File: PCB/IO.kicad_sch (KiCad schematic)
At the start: 34 parts, among them J501 Conn_02x03_Counter_Clockwise, J502 USB_C_Receptacle_USB2.0_16P, J503 Screw_Terminal_01x06, J504 Screw_Terminal_01x04, J505 Conn_01x04, J506 Conn_02x03_Counter_Clockwise, J507 Conn_01x06, Q1 SL2302S

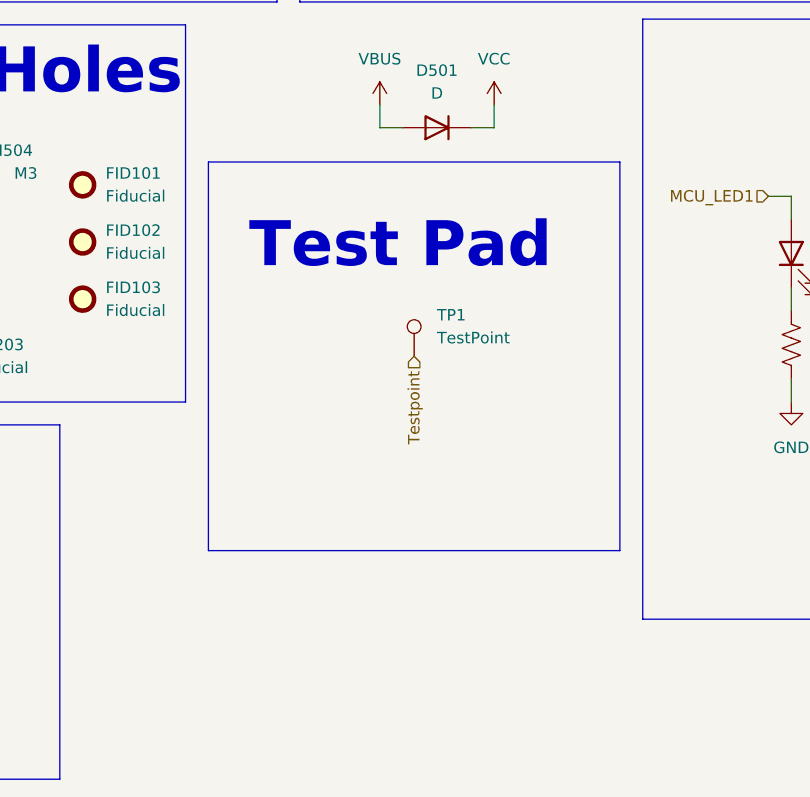
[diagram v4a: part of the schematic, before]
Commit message: Added DFU button and VCC pad by programming header
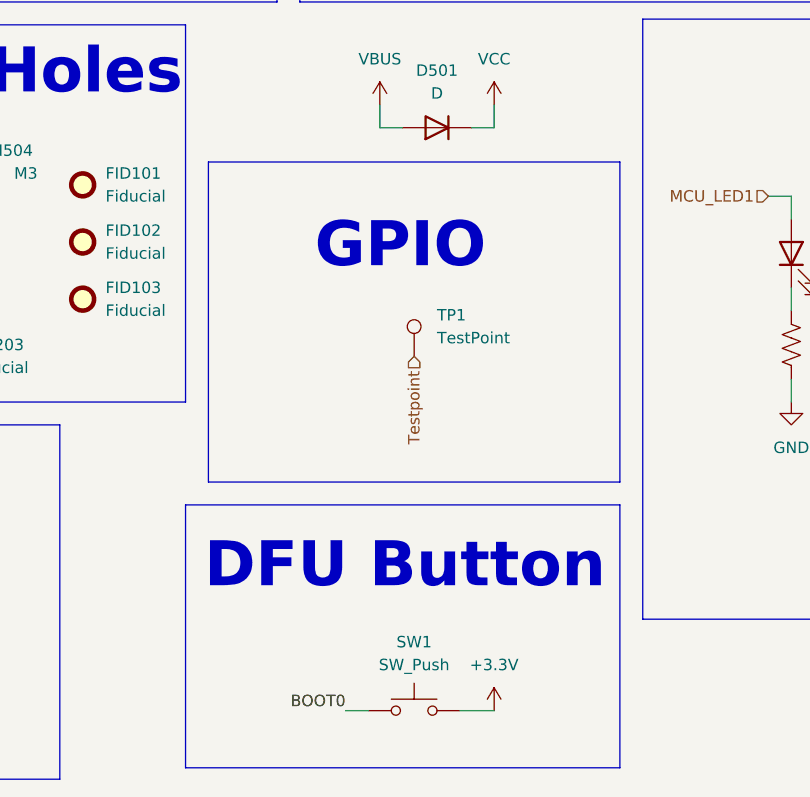
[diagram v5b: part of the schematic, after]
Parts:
- added SW1: SW_Push, imported:SW_1TS026A, symbol Switch:SW_Push
- TP1: footprint (none) -> TestPoint:TestPoint_Pad_D1.5mm
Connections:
- net +3.3V: now also SW1.2
- net BOOT0: now also SW1.1
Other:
- note added: "DFU Button"
- note added: "GPIO"
- note removed: "Test Pad"
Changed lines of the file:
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@@
 	(rectangle
 		(start 78.74 101.6)
-		(end 124.46 144.78)
+		(end 124.46 137.16)
 		(stroke
 			(width 0)
@@
 		)
 	)
+	(rectangle
+		(start 76.2 139.7)
+		(end 124.46 168.91)
+		(stroke
+			(width 0)
+			(type default)
+		)
+		(fill
+			(type none)
+		)
+	)
 	(text "Header"
 		(exclude_from_sim no)
@@
 		)
 	)
-	(text "Test Pad"
+	(text "GPIO"
 		(exclude_from_sim no)
 		(at 100.076 110.998 0)
@@
 		)
 	)
+	(text "DFU Button"
+		(exclude_from_sim no)
+		(at 100.584 146.558 0)
+		(effects
+			(font
+				(size 5 5)
+				(thickness 1)
+				(bold yes)
+			)
+		)
+	)
 	(text "Pyro Channels"
 		(exclude_from_sim no)
@@
 	(wire
 		(pts
+			(xy 106.68 162.56) (xy 110.49 162.56)
+		)
+		(stroke
+			(width 0)
+			(type default)
+		)
+	)
+	(wire
+		(pts
 			(xy 165.1 34.29) (xy 167.64 34.29)
 		)
@@
 	(wire
 		(pts
+			(xy 93.98 162.56) (xy 96.52 162.56)
+		)
+		(stroke
+			(width 0)
+			(type default)
+		)
+	)
+	(wire
+		(pts
 			(xy 74.93 53.34) (xy 72.39 53.34)
 		)
@@
 		)
 	)
+	(label "BOOT0"
+		(at 93.98 162.56 180)
+		(effects
+			(font
+				(size 1.27 1.27)
+			)
+			(justify right bottom)
+		)
+	)
 	(hierarchical_label "SWO"
 		(shape input)
@@
 	)
 	(symbol
+		(lib_id "power:+3.3V")
+		(at 110.49 162.56 0)
+		(unit 1)
+		(exclude_from_sim no)
+		(in_bom yes)
+		(on_board yes)
+		(dnp no)
+		(fields_autoplaced yes)
+		(property "Reference" "#PWR07"
+			(at 110.49 166.37 0)
+			(effects
+				(font
+					(size 1.27 1.27)
+				)
+				(hide yes)
+			)
+		)
+		(property "Value" "+3.3V"
+			(at 110.49 157.48 0)
+			(effects
+				(font
+					(size 1.27 1.27)
+				)
+			)
+		)
+		(property "Footprint" ""
+			(at 110.49 162.56 0)
+			(effects
+				(font
+					(size 1.27 1.27)
+				)
+				(hide yes)
+			)
+		)
+		(property "Datasheet" ""
+			(at 110.49 162.56 0)
+			(effects
+				(font
+					(size 1.27 1.27)
+				)
+				(hide yes)
+			)
+		)
+		(property "Description" "Power symbol creates a global label with name \"+3.3V\""
+			(at 110.49 162.56 0)
+			(effects
+				(font
+					(size 1.27 1.27)
+				)
+				(hide yes)
+			)
+		)
+		(pin "1"
+		)
+		(instances
+			(project "Flight Computer"
+				(path "/4254ccd1-49f4-4fe6-9bf7-ccb200d73af4/0a0b3d01-7422-42e0-b725-ff9e85b891ec"
+					(reference "#PWR07")
+					(unit 1)
+				)
+			)
+		)
+	)
+	(symbol
 		(lib_id "power:GND")
 		(at 36.83 110.49 0)
@@
 	)
 	(symbol
+		(lib_id "Switch:SW_Push")
+		(at 101.6 162.56 0)
+		(unit 1)
+		(exclude_from_sim no)
+		(in_bom yes)
+		(on_board yes)
+		(dnp no)
+		(fields_autoplaced yes)
+		(property "Reference" "SW1"
+			(at 101.6 154.94 0)
+			(effects
+				(font
+					(size 1.27 1.27)
+				)
+			)
+		)
+		(property "Value" "SW_Push"
+			(at 101.6 157.48 0)
+			(effects
+				(font
+					(size 1.27 1.27)
+				)
+			)
+		)
+		(property "Footprint" "imported:SW_1TS026A"
+			(at 101.6 157.48 0)
+			(effects
+				(font
+					(size 1.27 1.27)
+				)
+				(hide yes)
+			)
+		)
+		(property "Datasheet" "~"
+			(at 101.6 157.48 0)
+			(effects
+				(font
+					(size 1.27 1.27)
+				)
+				(hide yes)
+			)
+		)
+		(property "Description" "Push button switch, generic, two pins"
+			(at 101.6 162.56 0)
+			(effects
+				(font
+					(size 1.27 1.27)
+				)
+				(hide yes)
+			)
+		)
+		(pin "2"
+		)
+		(pin "1"
+		)
+		(instances
+			(project "Flight Computer"
+				(path "/4254ccd1-49f4-4fe6-9bf7-ccb200d73af4/0a0b3d01-7422-42e0-b725-ff9e85b891ec"
+					(reference "SW1")
+					(unit 1)
+				)
+			)
+		)
+	)
+	(symbol
 		(lib_id "Connector_Generic:Conn_01x06")
 		(at 27.94 154.94 0)
@@
 			)
 		)
-		(property "Footprint" ""
+		(property "Footprint" "TestPoint:TestPoint_Pad_D1.5mm"
 			(at 106.68 123.19 0)
 			(effects

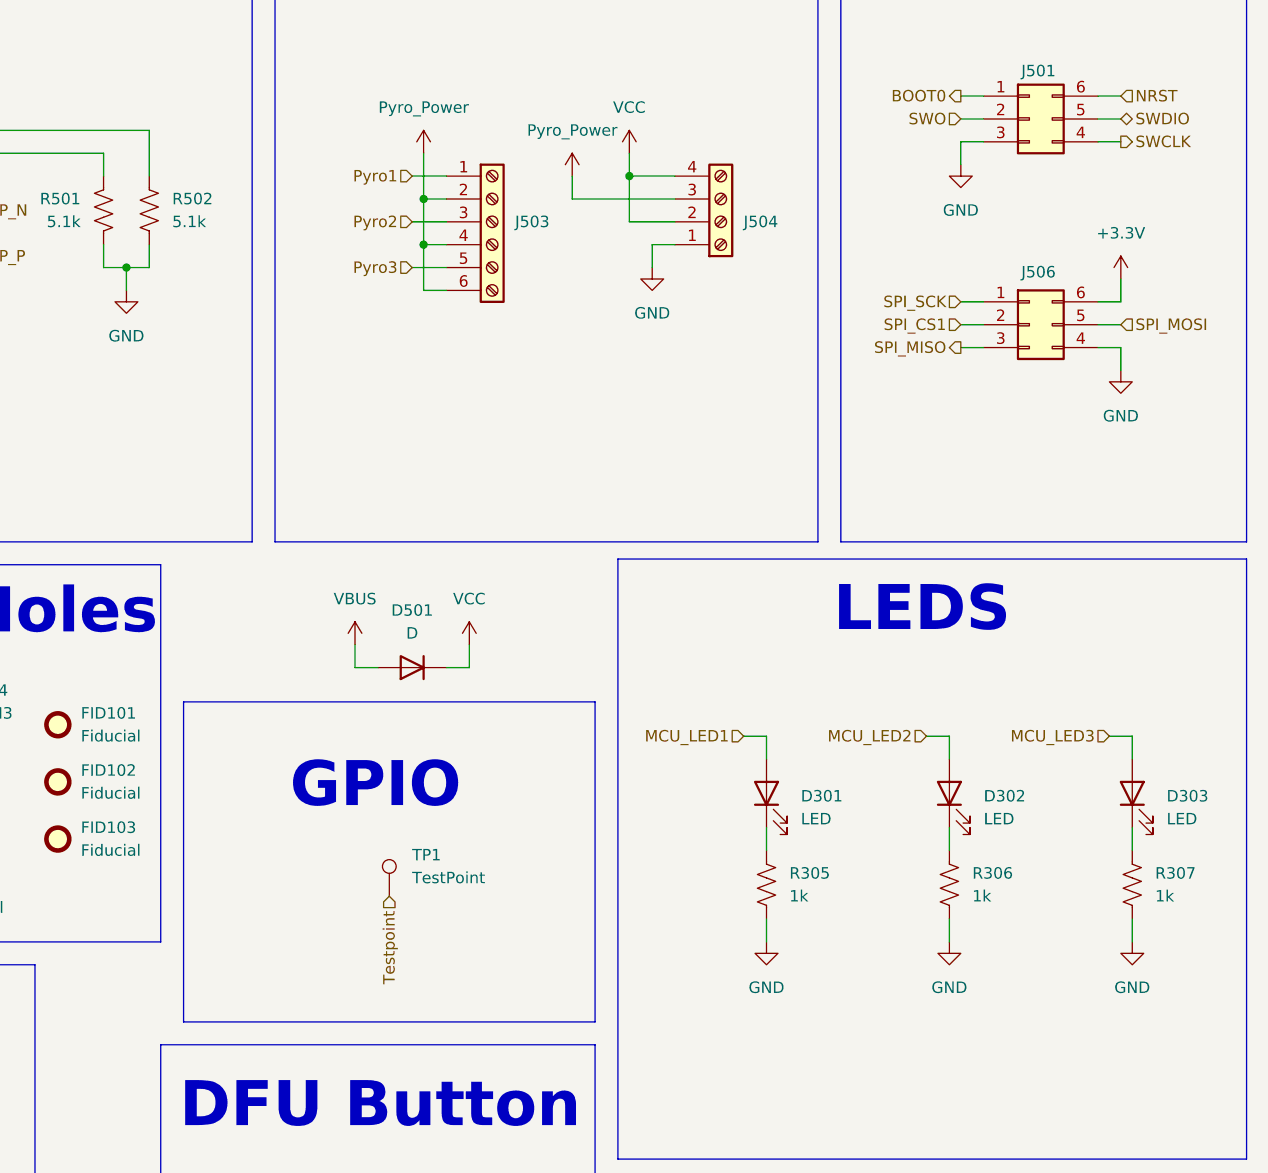
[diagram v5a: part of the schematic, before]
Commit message: Added two more GPIO test pads
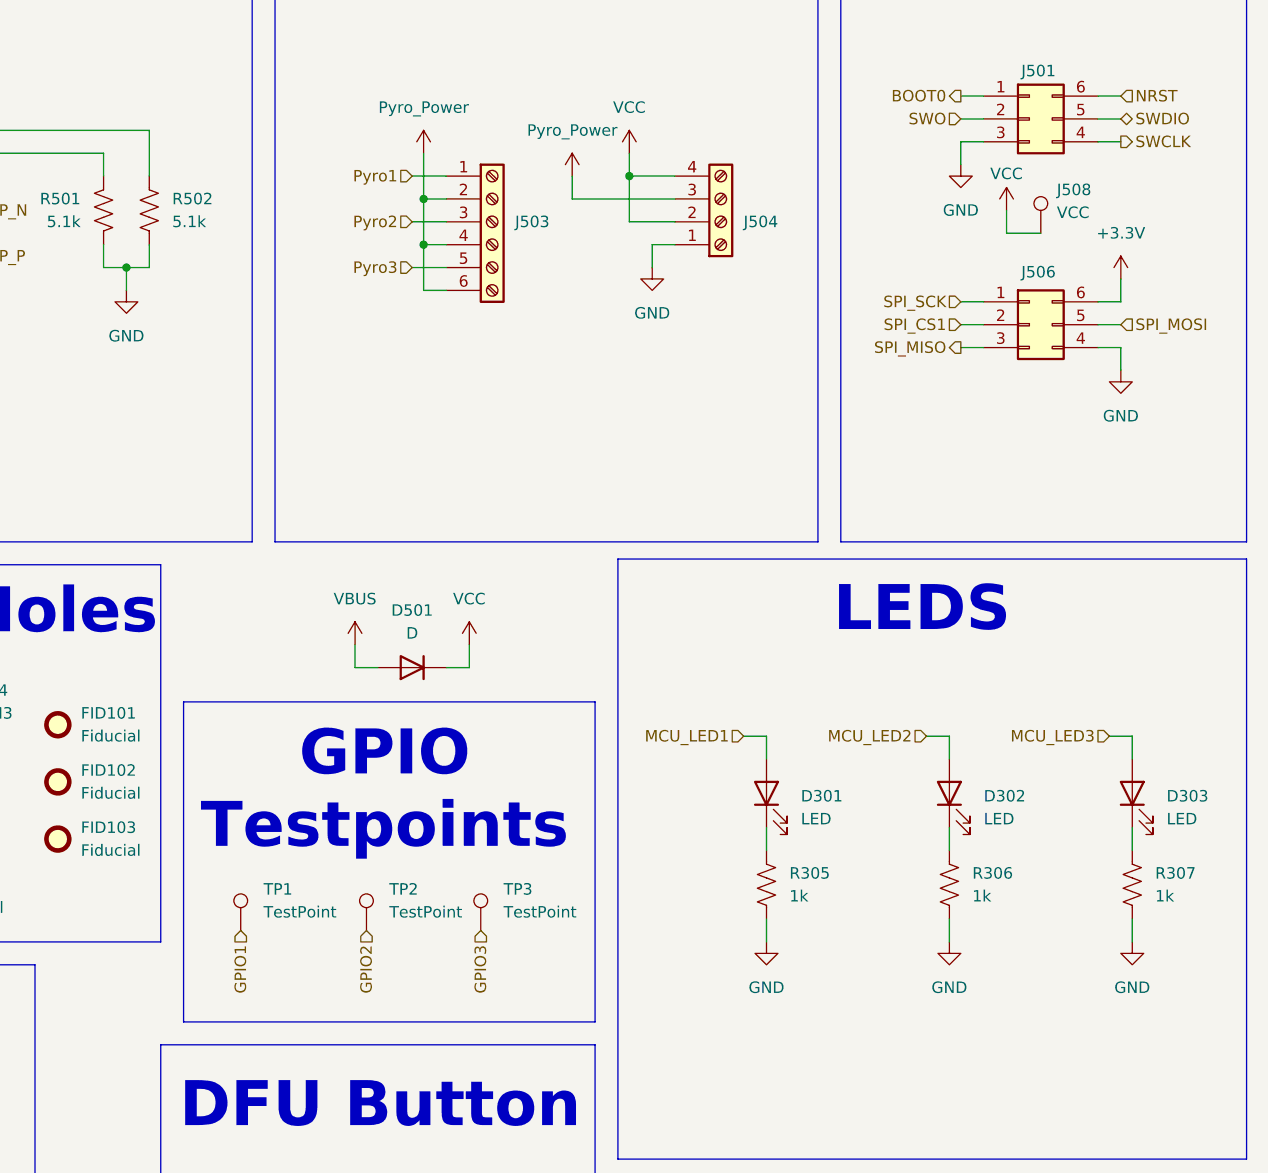
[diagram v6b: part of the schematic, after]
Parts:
- added J508: VCC, TestPoint:TestPoint_Pad_1.0x1.0mm, symbol Connector:TestPoint
- added TP2, TP3: TestPoint, TestPoint:TestPoint_Pad_D1.5mm, symbol Connector:TestPoint
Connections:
- net VCC: now also J508.1
- net Testpoint renamed GPIO1
- new net GPIO2: TP2.1
- new net GPIO3: TP3.1
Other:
- note added: "GPIO Testpoints"
- note removed: "GPIO"
- moved on the sheet: TP1

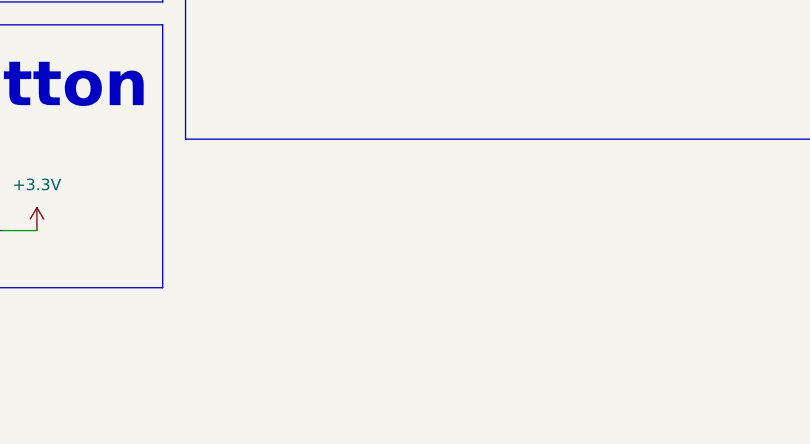
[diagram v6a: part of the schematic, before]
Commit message: Added Reset Button
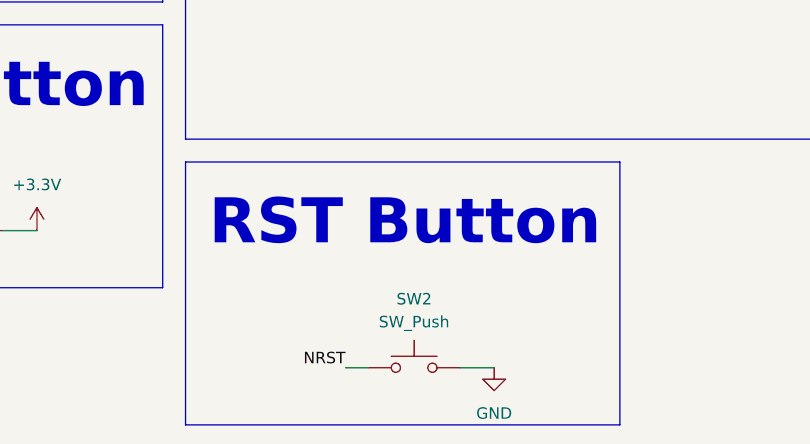
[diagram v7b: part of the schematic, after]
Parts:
- added SW2: SW_Push, imported:SW_1TS026A, symbol Switch:SW_Push
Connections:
- net GND: now also SW2.2
- net NRST: now also SW2.1
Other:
- note added: "RST Button"
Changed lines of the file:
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@@
 	)
 	(rectangle
+		(start 127 154.94)
+		(end 175.26 184.15)
+		(stroke
+			(width 0)
+			(type default)
+		)
+		(fill
+			(type none)
+		)
+	)
+	(rectangle
 		(start 151.765 14.605)
 		(end 196.85 83.82)
@@
 		)
 	)
+	(text "RST Button"
+		(exclude_from_sim no)
+		(at 151.384 161.798 0)
+		(effects
+			(font
+				(size 5 5)
+				(thickness 1)
+				(bold yes)
+			)
+		)
+	)
 	(text "Buzzer"
 		(exclude_from_sim no)
@@
 	(wire
 		(pts
+			(xy 157.48 177.8) (xy 161.29 177.8)
+		)
+		(stroke
+			(width 0)
+			(type default)
+		)
+	)
+	(wire
+		(pts
 			(xy 182.88 54.61) (xy 182.88 57.15)
 		)
@@
 	(wire
 		(pts
+			(xy 144.78 177.8) (xy 147.32 177.8)
+		)
+		(stroke
+			(width 0)
+			(type default)
+		)
+	)
+	(wire
+		(pts
 			(xy 220.98 48.26) (xy 223.52 48.26)
 		)
@@
 		)
 	)
+	(label "NRST"
+		(at 144.78 177.8 180)
+		(effects
+			(font
+				(size 1.27 1.27)
+			)
+			(justify right bottom)
+		)
+	)
 	(label "BOOT0"
 		(at 93.98 162.56 180)
@@
 		)
 		(instances
-			(project ""
+			(project "Flight Computer"
 				(path "/4254ccd1-49f4-4fe6-9bf7-ccb200d73af4/0a0b3d01-7422-42e0-b725-ff9e85b891ec"
 					(reference "J501")
@@
 		)
 		(instances
-			(project ""
+			(project "Flight Computer"
 				(path "/4254ccd1-49f4-4fe6-9bf7-ccb200d73af4/0a0b3d01-7422-42e0-b725-ff9e85b891ec"
 					(reference "BZ501")
@@
 		)
 		(instances
-			(project ""
+			(project "Flight Computer"
 				(path "/4254ccd1-49f4-4fe6-9bf7-ccb200d73af4/0a0b3d01-7422-42e0-b725-ff9e85b891ec"
 					(reference "#PWR0501")
@@
 		)
 		(instances
-			(project ""
+			(project "Flight Computer"
 				(path "/4254ccd1-49f4-4fe6-9bf7-ccb200d73af4/0a0b3d01-7422-42e0-b725-ff9e85b891ec"
 					(reference "G501")
@@
 		)
 		(instances
-			(project ""
+			(project "Flight Computer"
 				(path "/4254ccd1-49f4-4fe6-9bf7-ccb200d73af4/0a0b3d01-7422-42e0-b725-ff9e85b891ec"
 					(reference "J502")
@@
 		)
 		(instances
-			(project ""
+			(project "Flight Computer"
 				(path "/4254ccd1-49f4-4fe6-9bf7-ccb200d73af4/0a0b3d01-7422-42e0-b725-ff9e85b891ec"
 					(reference "J503")
@@
 		)
 		(instances
-			(project ""
+			(project "Flight Computer"
 				(path "/4254ccd1-49f4-4fe6-9bf7-ccb200d73af4/0a0b3d01-7422-42e0-b725-ff9e85b891ec"
 					(reference "R503")
@@
 		)
 		(instances
-			(project ""
+			(project "Flight Computer"
 				(path "/4254ccd1-49f4-4fe6-9bf7-ccb200d73af4/0a0b3d01-7422-42e0-b725-ff9e85b891ec"
 					(reference "#PWR0508")
@@
 	)
 	(symbol
+		(lib_id "Switch:SW_Push")
+		(at 152.4 177.8 0)
+		(unit 1)
+		(exclude_from_sim no)
+		(in_bom yes)
+		(on_board yes)
+		(dnp no)
+		(fields_autoplaced yes)
+		(property "Reference" "SW2"
+			(at 152.4 170.18 0)
+			(effects
+				(font
+					(size 1.27 1.27)
+				)
+			)
+		)
+		(property "Value" "SW_Push"
+			(at 152.4 172.72 0)
+			(effects
+				(font
+					(size 1.27 1.27)
+				)
+			)
+		)
+		(property "Footprint" "imported:SW_1TS026A"
+			(at 152.4 172.72 0)
+			(effects
+				(font
+					(size 1.27 1.27)
+				)
+				(hide yes)
+			)
+		)
+		(property "Datasheet" "~"
+			(at 152.4 172.72 0)
+			(effects
+				(font
+					(size 1.27 1.27)
+				)
+				(hide yes)
+			)
+		)
+		(property "Description" "Push button switch, generic, two pins"
+			(at 152.4 177.8 0)
+			(effects
+				(font
+					(size 1.27 1.27)
+				)
+				(hide yes)
+			)
+		)
+		(pin "2"
+		)
+		(pin "1"
+		)
+		(instances
+			(project "Flight Computer"
+				(path "/4254ccd1-49f4-4fe6-9bf7-ccb200d73af4/0a0b3d01-7422-42e0-b725-ff9e85b891ec"
+					(reference "SW2")
+					(unit 1)
+				)
+			)
+		)
+	)
+	(symbol
 		(lib_id "Connector:TestPoint")
 		(at 85.09 127 0)
@@
 		)
 		(instances
-			(project ""
+			(project "Flight Computer"
 				(path "/4254ccd1-49f4-4fe6-9bf7-ccb200d73af4/0a0b3d01-7422-42e0-b725-ff9e85b891ec"
 					(reference "TP1")
@@
 		)
 		(instances
-			(project ""
+			(project "Flight Computer"
 				(path "/4254ccd1-49f4-4fe6-9bf7-ccb200d73af4/0a0b3d01-7422-42e0-b725-ff9e85b891ec"
 					(reference "J508")
@@
 	)
 	(symbol
+		(lib_id "power:GND")
+		(at 161.29 177.8 0)
+		(unit 1)
+		(exclude_from_sim no)
+		(in_bom yes)
+		(on_board yes)
+		(dnp no)
+		(fields_autoplaced yes)
+		(property "Reference" "#PWR09"
+			(at 161.29 184.15 0)
+			(effects
+				(font
+					(size 1.27 1.27)
+				)
+				(hide yes)
+			)
+		)
+		(property "Value" "GND"
+			(at 161.29 182.88 0)
+			(effects
+				(font
+					(size 1.27 1.27)
+				)
+			)
+		)
+		(property "Footprint" ""
+			(at 161.29 177.8 0)
+			(effects
+				(font
+					(size 1.27 1.27)
+				)
+				(hide yes)
+			)
+		)
+		(property "Datasheet" ""
+			(at 161.29 177.8 0)
+			(effects
+				(font
+					(size 1.27 1.27)
+				)
+				(hide yes)
+			)
+		)
+		(property "Description" "Power symbol creates a global label with name \"GND\" , ground"
+			(at 161.29 177.8 0)
+			(effects
+				(font
+					(size 1.27 1.27)
+				)
+				(hide yes)
+			)
+		)
+		(pin "1"
+		)
+		(instances
+			(project "Flight Computer"
+				(path "/4254ccd1-49f4-4fe6-9bf7-ccb200d73af4/0a0b3d01-7422-42e0-b725-ff9e85b891ec"
+					(reference "#PWR09")
+					(unit 1)
+				)
+			)
+		)
+	)
+	(symbol
 		(lib_id "Device:D")
 		(at 104.14 97.79 180)
@@
 		)
 		(instances
-			(project ""
+			(project "Flight Computer"
 				(path "/4254ccd1-49f4-4fe6-9bf7-ccb200d73af4/0a0b3d01-7422-42e0-b725-ff9e85b891ec"
 					(reference "D501")
@@
 		)
 		(instances
-			(project ""
+			(project "Flight Computer"
 				(path "/4254ccd1-49f4-4fe6-9bf7-ccb200d73af4/0a0b3d01-7422-42e0-b725-ff9e85b891ec"
 					(reference "D502")
